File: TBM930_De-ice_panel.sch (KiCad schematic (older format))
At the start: 91 parts, among them J1 SW_AIRFRAME_DE_ICE, J10 AVR-ISP-6, J11 Screw_Terminal_01x02, J2 SW_ICE_LIGHT, J3 SW_PROP_DE_ICE, J4 SW_WIND_SHIELD, J5 SW_PITOT_L_HTR, J6 SW_PITOT_R_HTR, J7 SW_INERT_SEP, J8 Barrel_Jack, J9 USB_B_Mini, SW1 SW_Push, SW2 SW_Push, U1 TLC5917IN, U2 TLC5917IN, U3 ATmega32U4-MU, Y1 Crystal_GND24

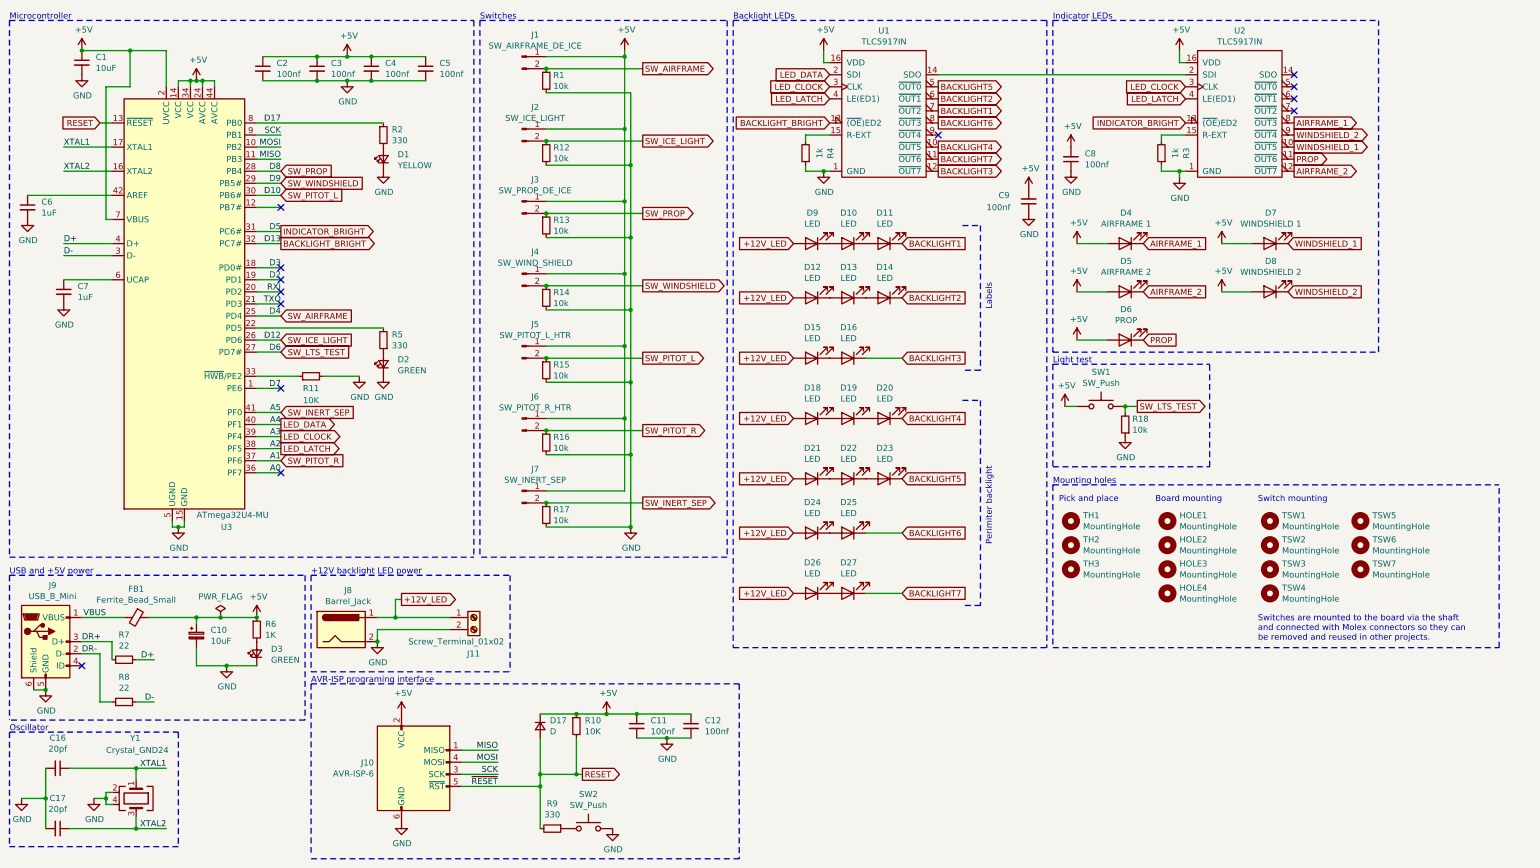
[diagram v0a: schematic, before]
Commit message: Fix switches back to ground connection (#4)
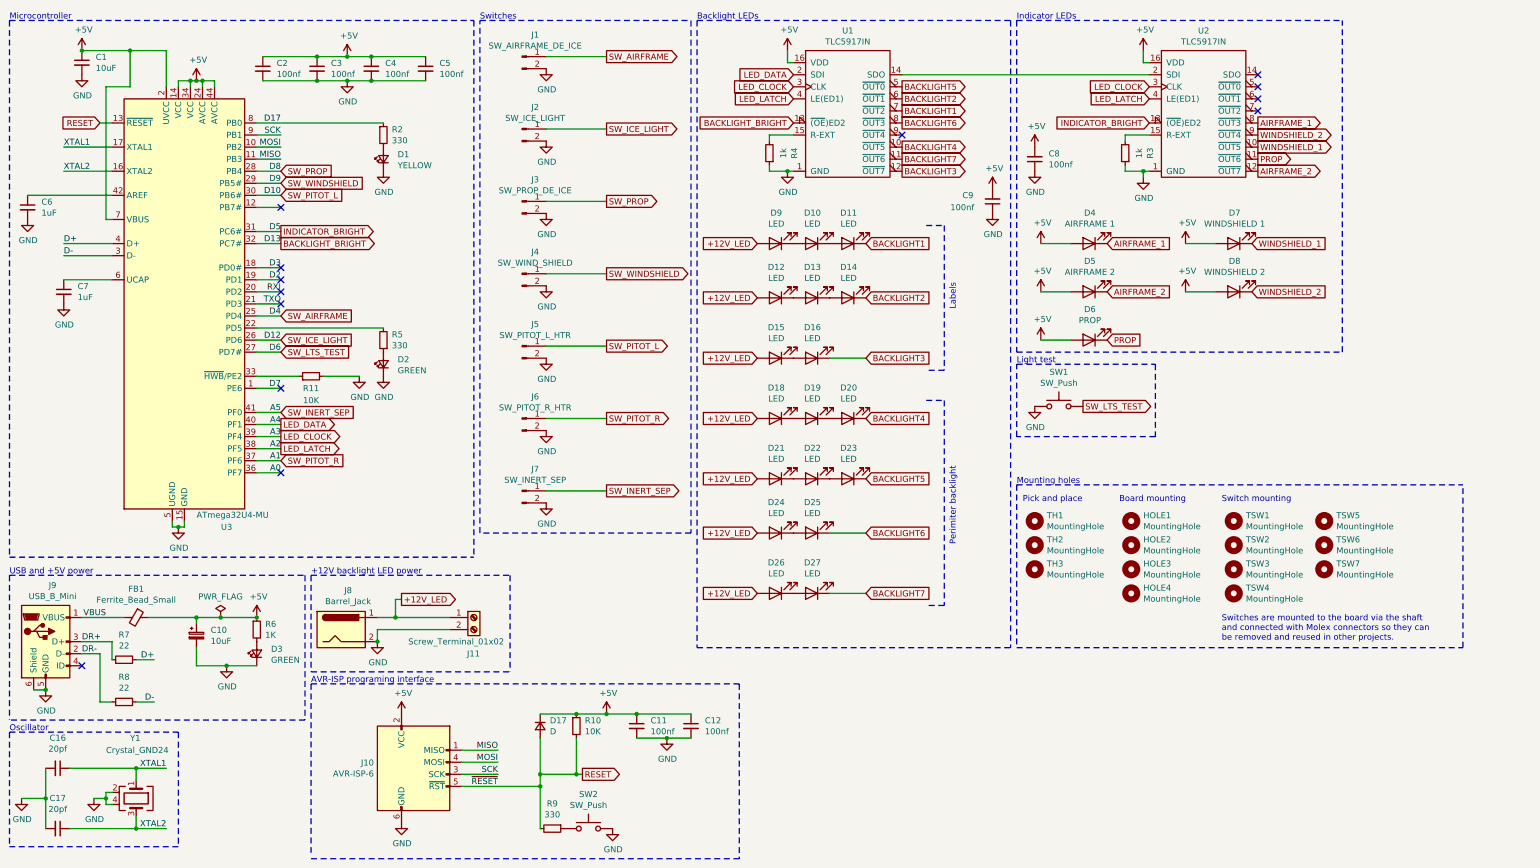
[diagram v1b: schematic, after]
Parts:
- removed R1, R12, R13, R14, R15, R16, R17, R18: 10k, Resistor_SMD:R_0402_1005Metric, symbol Device:R_Small
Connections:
- net +5V: no longer J1.1 (Pin_1), J2.1 (Pin_1), J3.1 (Pin_1), J4.1 (Pin_1), J5.1 (Pin_1), J6.1 (Pin_1), J7.1 (Pin_1), SW1.1
- net GND: now also J1.2 (Pin_2), J2.2 (Pin_2), J3.2 (Pin_2), J4.2 (Pin_2), J5.2 (Pin_2), J6.2 (Pin_2), J7.2 (Pin_2), SW1.1
- net SW_AIRFRAME: now also J1.1 (Pin_1); no longer J1.2 (Pin_2)
- net SW_ICE_LIGHT: now also J2.1 (Pin_1); no longer J2.2 (Pin_2)
- net SW_INERT_SEP: now also J7.1 (Pin_1); no longer J7.2 (Pin_2)
- net SW_PITOT_L: now also J5.1 (Pin_1); no longer J5.2 (Pin_2)
- net SW_PITOT_R: now also J6.1 (Pin_1); no longer J6.2 (Pin_2)
- net SW_PROP: now also J3.1 (Pin_1); no longer J3.2 (Pin_2)
- net SW_WINDSHIELD: now also J4.1 (Pin_1); no longer J4.2 (Pin_2)
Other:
- moved on the sheet: C8, C9, D10, D11, D12, D13, D14, D15, D16, D18, D19, D20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
